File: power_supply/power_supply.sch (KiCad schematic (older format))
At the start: 16 parts, among them J1 Conn_01x02_Female, J6 Conn_01x02_Male, J7 Conn_01x02_Male, T1 Transformer_1P_2S

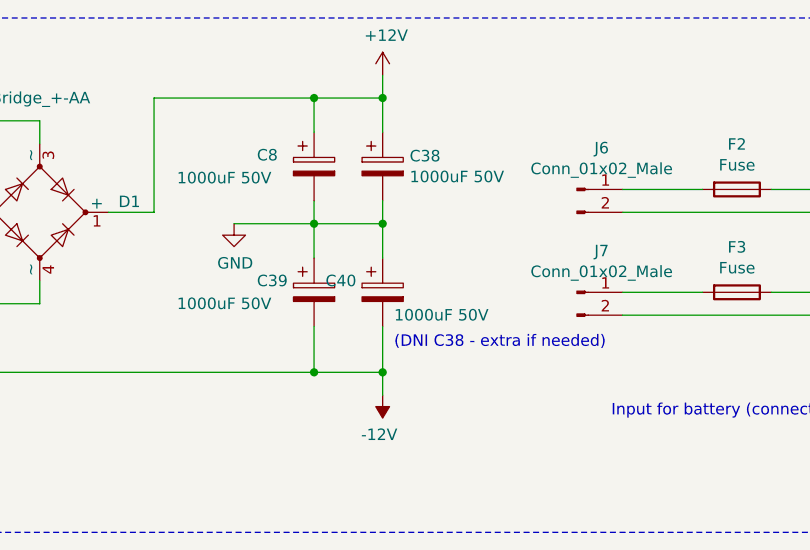
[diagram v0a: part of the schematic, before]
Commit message: Moved power supply off preamp
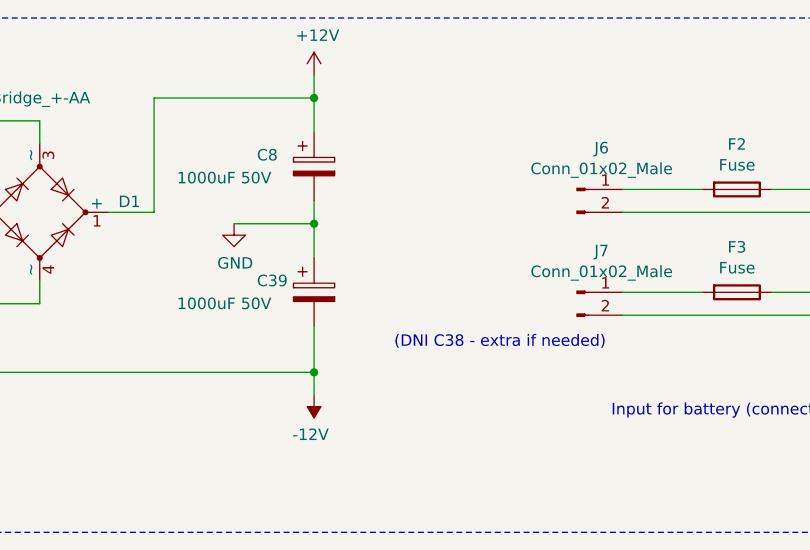
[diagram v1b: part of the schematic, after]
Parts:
- removed C38, C40: 1000uF 50V, Capacitor_THT:CP_Radial_D17.0mm_P7.50mm, symbol Device:CP
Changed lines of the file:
@@
 Wire Wire Line
 	5600 2000 5600 2200
-Wire Wire Line
-	5600 2200 5900 2200
 $Comp
 L Device:Transformer_1P_2S T1
@@
 L power:+12V #PWR0102
 U 1 1 5D654E8A
-P 5900 900
-F 0 "#PWR0102" H 5900 750 50  0001 C CNN
-F 1 "+12V" H 5915 1073 50  0000 C CNN
-F 2 "" H 5900 900 50  0001 C CNN
-F 3 "" H 5900 900 50  0001 C CNN
-	1    5900 900
+P 5600 900
+F 0 "#PWR0102" H 5600 750 50  0001 C CNN
+F 1 "+12V" H 5615 1073 50  0000 C CNN
+F 2 "" H 5600 900 50  0001 C CNN
+F 3 "" H 5600 900 50  0001 C CNN
+	1    5600 900
 	1    0    0    -1
 $EndComp
@@
 L power:-12V #PWR0103
 U 1 1 5D6561DF
-P 5900 2300
-F 0 "#PWR0103" H 5900 2400 50  0001 C CNN
-F 1 "-12V" H 5915 2473 50  0000 C CNN
-F 2 "" H 5900 2300 50  0001 C CNN
-F 3 "" H 5900 2300 50  0001 C CNN
-	1    5900 2300
+P 5600 2300
+F 0 "#PWR0103" H 5600 2400 50  0001 C CNN
+F 1 "-12V" H 5615 2473 50  0000 C CNN
+F 2 "" H 5600 2300 50  0001 C CNN
+F 3 "" H 5600 2300 50  0001 C CNN
+	1    5600 2300
 	-1   0    0    1
 $EndComp
@@
 	0    1    1    0
 $EndComp
-Connection ~ 5600 2200
 Wire Wire Line
 	6950 1400 7300 1400
@@
 Wire Wire Line
 	6950 1950 7850 1950
-$Comp
-L Device:CP C38
-U 1 1 5E1D3B0E
-P 5900 1300
-F 0 "C38" H 6018 1346 50  0000 L CNN
-F 1 "1000uF 50V" H 6018 1255 50  0000 L CNN
-F 2 "Capacitor_THT:CP_Radial_D17.0mm_P7.50mm" H 5938 1150 50  0001 C CNN
-F 3 "~" H 5900 1300 50  0001 C CNN
-	1    5900 1300
-	1    0    0    -1
-$EndComp
 Text Notes 5950 2100 0    50   ~ 0
 (DNI C38 - extra if needed)
-Wire Wire Line
-	5900 2000 5900 2200
-Connection ~ 5900 2200
-Wire Wire Line
-	5900 2300 5900 2200
 Wire Wire Line
 	4700 1500 4900 1500
@@
 	1    0    0    -1
 $EndComp
-$Comp
-L Device:CP C40
-U 1 1 5E00BF29
-P 5900 1850
-F 0 "C40" H 5650 1900 50  0000 L CNN
-F 1 "1000uF 50V" H 5950 1750 50  0000 L CNN
-F 2 "Capacitor_THT:CP_Radial_D17.0mm_P7.50mm" H 5938 1700 50  0001 C CNN
-F 3 "~" H 5900 1850 50  0001 C CNN
-	1    5900 1850
-	1    0    0    -1
-$EndComp
-Wire Wire Line
-	5900 1450 5900 1550
 Wire Wire Line
 	5600 1700 5600 1550
 Wire Wire Line
-	5900 1000 5900 1150
-Wire Wire Line
 	5600 1150 5600 1000
-Connection ~ 5600 1000
-Wire Wire Line
-	5600 1000 5900 1000
 $Comp
 L power:GND #PWR0215
@@
 Wire Wire Line
 	5600 1550 5600 1450
-Wire Wire Line
-	5600 1550 5900 1550
-Connection ~ 5900 1550
-Wire Wire Line
-	5900 1550 5900 1700
-Wire Wire Line
-	5900 900  5900 1000
-Connection ~ 5900 1000
 Wire Wire Line
 	4900 1000 5600 1000
@@
 Wire Notes Line
 	750  650  750  2900
+Connection ~ 5600 2200
+Wire Wire Line
+	5600 2300 5600 2200
+Wire Wire Line
+	5600 1000 5600 900
+Connection ~ 5600 1000
 $EndSCHEMATC

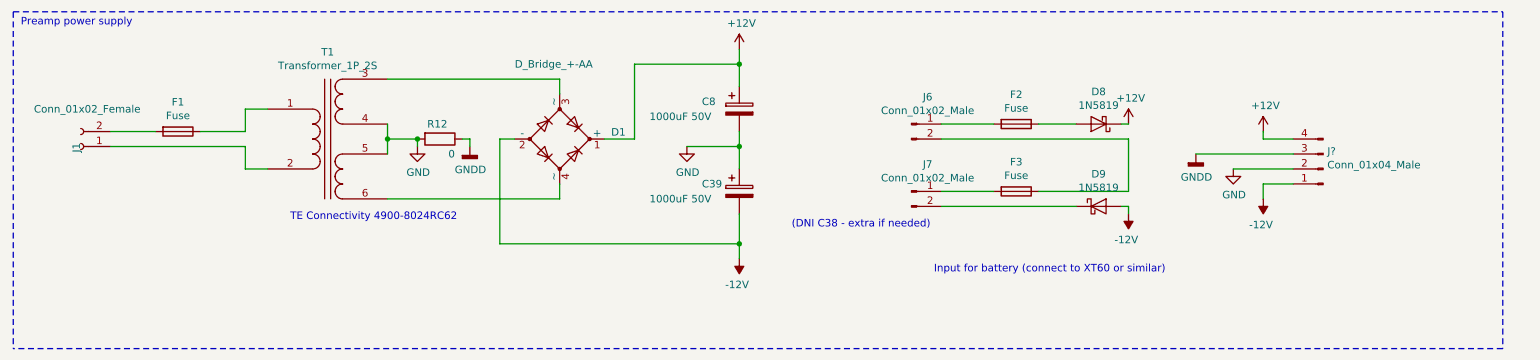
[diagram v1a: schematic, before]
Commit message: Added top-side ground plane, started power supply work
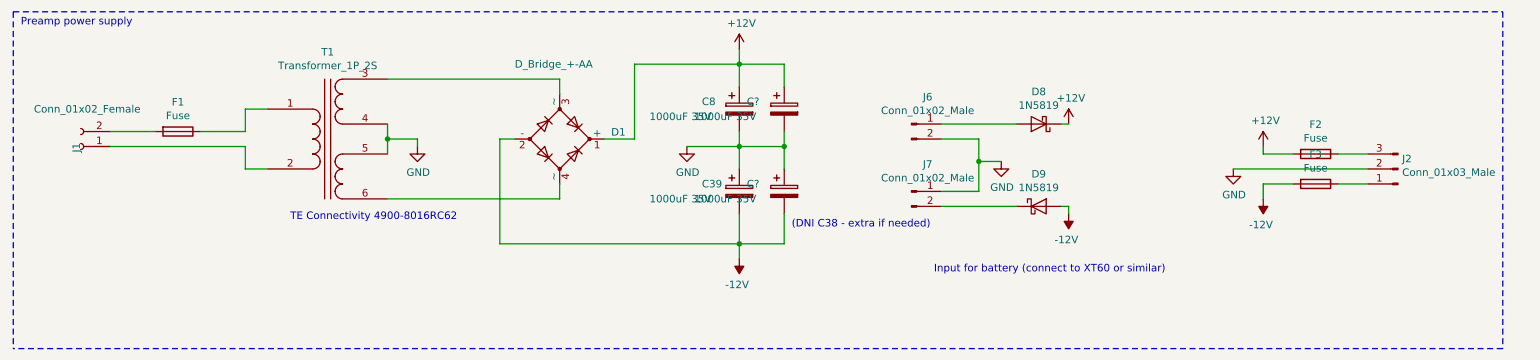
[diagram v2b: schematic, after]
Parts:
- removed J?: Conn_01x04_Male, symbol Connector:Conn_01x04_Male
- removed R12: 0, Resistor_THT:R_Axial_DIN0207_L6.3mm_D2.5mm_P10.16mm_Horizontal, symbol Device:R
- added C? (x2): 1000uF 35V, Capacitor_THT:CP_Radial_D10.0mm_P5.00mm, symbol Device:CP
- added J2: Conn_01x03_Male, Connector_PinHeader_2.54mm:PinHeader_1x03_P2.54mm_Vertical, symbol Connector:Conn_01x03_Male
- C39, C8: value 1000uF 50V -> 1000uF 35V; footprint Capacitor_THT:CP_Radial_D17.0mm_P7.50mm -> Capacitor_THT:CP_Radial_D10.0mm_P5.00mm
- D1: footprint (none) -> Project-152-Bass-Guitar-Amp.pretty:DiodesIncDF-M
- F2, F3: footprint (none) -> Fuse:Fuseholder_Blade_Mini_Keystone_3568
- T1: footprint Project-152-Bass-Guitar-Amp:TE 49008024RC62 -> Project-152-Bass-Guitar-Amp.pretty:TE490080XXRC62
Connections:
- net +12V: now also F2.2, C?.1
- net -12V: now also F3.2, C?.2
- net GND: now also J6.2 (Pin_2), J7.1 (Pin_1), C?.1, C?.2, J2.2 (Pin_2)
- net at J6.1 (Pin_1): now also D8.2 (A); no longer F2.2
- net at F3.1: now also J2.1 (Pin_1); no longer J6.2 (Pin_2)
- net at F2.1: now also J2.3 (Pin_3); no longer D8.2 (A)
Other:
- note added: "TE Connectivity 4900-8016RC62"
- note removed: "TE Connectivity 4900-8024RC62"
- moved on the sheet: D8, D9, F2, F3
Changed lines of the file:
@@
 F 0 "D1" H 4744 1546 50  0000 L CNN
 F 1 "D_Bridge_+-AA" H 4100 2000 50  0000 L CNN
-F 2 "" H 4400 1500 50  0001 C CNN
+F 2 "Project-152-Bass-Guitar-Amp.pretty:DiodesIncDF-M" H 4400 1500 50  0001 C CNN
 F 3 "~" H 4400 1500 50  0001 C CNN
 	1    4400 1500
@@
 	4000 1500 4000 2200
 Text Notes 2600 2050 0    50   ~ 0
-TE Connectivity 4900-8024RC62
+TE Connectivity 4900-8016RC62
 $Comp
 L Connector:Conn_01x02_Female J1
@@
 P 5600 1300
 F 0 "C8" H 5350 1350 50  0000 L CNN
-F 1 "1000uF 50V" H 5000 1250 50  0000 L CNN
-F 2 "Capacitor_THT:CP_Radial_D17.0mm_P7.50mm" H 5638 1150 50  0001 C CNN
+F 1 "1000uF 35V" H 5000 1250 50  0000 L CNN
+F 2 "Capacitor_THT:CP_Radial_D10.0mm_P5.00mm" H 5638 1150 50  0001 C CNN
 F 3 "~" H 5600 1300 50  0001 C CNN
 	1    5600 1300
@@
 F 0 "T1" H 2850 2081 50  0000 C CNN
 F 1 "Transformer_1P_2S" H 2850 1990 50  0000 C CNN
-F 2 "Project-152-Bass-Guitar-Amp:TE 49008024RC62" H 2850 1500 50  0001 C CNN
+F 2 "Project-152-Bass-Guitar-Amp.pretty:TE490080XXRC62" H 2850 1500 50  0001 C CNN
 F 3 "~" H 2850 1500 50  0001 C CNN
 	1    2850 1500
@@
 	1    0    0    -1
 $EndComp
-Wire Wire Line
-	8200 1500 8200 1850
 $Comp
 L power:+12V #PWR0118
 U 1 1 5D6AE19B
-P 8200 1400
-F 0 "#PWR0118" H 8200 1250 50  0001 C CNN
-F 1 "+12V" H 8215 1573 50  0000 C CNN
-F 2 "" H 8200 1400 50  0001 C CNN
-F 3 "" H 8200 1400 50  0001 C CNN
-	1    8200 1400
+P 7800 1400
+F 0 "#PWR0118" H 7800 1250 50  0001 C CNN
+F 1 "+12V" H 7815 1573 50  0000 C CNN
+F 2 "" H 7800 1400 50  0001 C CNN
+F 3 "" H 7800 1400 50  0001 C CNN
+	1    7800 1400
 	1    0    0    -1
 $EndComp
@@
 L power:-12V #PWR0119
 U 1 1 5D6AED97
-P 8200 2000
-F 0 "#PWR0119" H 8200 2100 50  0001 C CNN
-F 1 "-12V" H 8215 2173 50  0000 C CNN
-F 2 "" H 8200 2000 50  0001 C CNN
-F 3 "" H 8200 2000 50  0001 C CNN
-	1    8200 2000
-	-1   0    0    1
-$EndComp
-Wire Wire Line
-	8200 1950 8200 2000
-Wire Wire Line
-	7600 1850 8200 1850
-Wire Wire Line
-	7600 1400 7850 1400
+P 7800 2000
+F 0 "#PWR0119" H 7800 2100 50  0001 C CNN
+F 1 "-12V" H 7815 2173 50  0000 C CNN
+F 2 "" H 7800 2000 50  0001 C CNN
+F 3 "" H 7800 2000 50  0001 C CNN
+	1    7800 2000
+	-1   0    0    1
+$EndComp
+Wire Wire Line
+	7800 1950 7800 2000
 Text Notes 6900 2400 0    50   ~ 0
 Input for battery (connect to XT60 or similar)
 Wire Wire Line
-	8150 1950 8200 1950
+	7750 1950 7800 1950
 $Comp
 L Diode:1N5819 D8
 U 1 1 5D6CDB80
-P 8000 1400
-F 0 "D8" H 8000 1184 50  0000 C CNN
-F 1 "1N5819" H 8000 1275 50  0000 C CNN
-F 2 "Diode_THT:D_DO-41_SOD81_P10.16mm_Horizontal" H 8000 1225 50  0001 C CNN
-F 3 "http://www.vishay.com/docs/88525/1n5817.pdf" H 8000 1400 50  0001 C CNN
-	1    8000 1400
+P 7600 1400
+F 0 "D8" H 7600 1184 50  0000 C CNN
+F 1 "1N5819" H 7600 1275 50  0000 C CNN
+F 2 "Diode_THT:D_DO-41_SOD81_P10.16mm_Horizontal" H 7600 1225 50  0001 C CNN
+F 3 "http://www.vishay.com/docs/88525/1n5817.pdf" H 7600 1400 50  0001 C CNN
+	1    7600 1400
 	-1   0    0    1
 $EndComp
@@
 L Diode:1N5819 D9
 U 1 1 5D6CF15E
-P 8000 1950
-F 0 "D9" H 8000 2166 50  0000 C CNN
-F 1 "1N5819" H 8000 2075 50  0000 C CNN
-F 2 "Diode_THT:D_DO-41_SOD81_P10.16mm_Horizontal" H 8000 1775 50  0001 C CNN
-F 3 "http://www.vishay.com/docs/88525/1n5817.pdf" H 8000 1950 50  0001 C CNN
-	1    8000 1950
-	1    0    0    -1
-$EndComp
-Wire Wire Line
-	8200 1400 8150 1400
+P 7600 1950
+F 0 "D9" H 7600 2166 50  0000 C CNN
+F 1 "1N5819" H 7600 2075 50  0000 C CNN
+F 2 "Diode_THT:D_DO-41_SOD81_P10.16mm_Horizontal" H 7600 1775 50  0001 C CNN
+F 3 "http://www.vishay.com/docs/88525/1n5817.pdf" H 7600 1950 50  0001 C CNN
+	1    7600 1950
+	1    0    0    -1
+$EndComp
+Wire Wire Line
+	7800 1400 7750 1400
 Text Notes 800  750  0    50   ~ 0
 Preamp power supply
@@
 	1400 1550 2300 1550
 $Comp
-L power:GNDD #PWR0145
-U 1 1 5D854759
-P 3800 1550
-F 0 "#PWR0145" H 3800 1300 50  0001 C CNN
-F 1 "GNDD" H 3804 1395 50  0000 C CNN
-F 2 "" H 3800 1550 50  0001 C CNN
-F 3 "" H 3800 1550 50  0001 C CNN
-	1    3800 1550
-	1    0    0    -1
-$EndComp
-Wire Wire Line
-	3800 1500 3800 1550
-$Comp
-L Device:R R12
-U 1 1 5D8EA5F3
-P 3600 1500
-F 0 "R12" V 3500 1550 50  0000 R CNN
-F 1 "0" V 3700 1600 50  0000 R CNN
-F 2 "Resistor_THT:R_Axial_DIN0207_L6.3mm_D2.5mm_P10.16mm_Horizontal" V 3530 1500 50  0001 C CNN
-F 3 "~" H 3600 1500 50  0001 C CNN
-	1    3600 1500
-	0    1    1    0
-$EndComp
-Connection ~ 3450 1500
-Wire Wire Line
-	3750 1500 3800 1500
-$Comp
 L Device:Fuse F2
 U 1 1 5E48268A
-P 7450 1400
-F 0 "F2" V 7253 1400 50  0000 C CNN
-F 1 "Fuse" V 7344 1400 50  0000 C CNN
-F 2 "" V 7380 1400 50  0001 C CNN
-F 3 "~" H 7450 1400 50  0001 C CNN
-	1    7450 1400
+P 9450 1600
+F 0 "F2" V 9253 1600 50  0000 C CNN
+F 1 "Fuse" V 9344 1600 50  0000 C CNN
+F 2 "Fuse:Fuseholder_Blade_Mini_Keystone_3568" V 9380 1600 50  0001 C CNN
+F 3 "~" H 9450 1600 50  0001 C CNN
+	1    9450 1600
 	0    1    1    0
 $EndComp
@@
 L Device:Fuse F3
 U 1 1 5E4FFBD7
-P 7450 1850
-F 0 "F3" V 7253 1850 50  0000 C CNN
-F 1 "Fuse" V 7344 1850 50  0000 C CNN
-F 2 "" V 7380 1850 50  0001 C CNN
-F 3 "~" H 7450 1850 50  0001 C CNN
-	1    7450 1850
+P 9450 1800
+F 0 "F3" V 9253 1800 50  0000 C CNN
+F 1 "Fuse" V 9344 1800 50  0000 C CNN
+F 2 "Fuse:Fuseholder_Blade_Mini_Keystone_3568" V 9380 1800 50  0001 C CNN
+F 3 "~" H 9450 1800 50  0001 C CNN
+	1    9450 1800
 	0    1    1    0
 $EndComp
-Wire Wire Line
-	6950 1400 7300 1400
-Wire Wire Line
-	6950 1500 8200 1500
-Wire Wire Line
-	6950 1850 7300 1850
-Wire Wire Line
-	6950 1950 7850 1950
 Text Notes 5950 2100 0    50   ~ 0
 (DNI C38 - extra if needed)
@@
 P 5600 1850
 F 0 "C39" H 5350 1900 50  0000 L CNN
-F 1 "1000uF 50V" H 5000 1800 50  0000 L CNN
-F 2 "Capacitor_THT:CP_Radial_D17.0mm_P7.50mm" H 5638 1700 50  0001 C CNN
+F 1 "1000uF 35V" H 5000 1800 50  0000 L CNN
+F 2 "Capacitor_THT:CP_Radial_D10.0mm_P5.00mm" H 5638 1700 50  0001 C CNN
 F 3 "~" H 5600 1850 50  0001 C CNN
 	1    5600 1850
@@
 	4000 2200 5600 2200
 $Comp
-L Connector:Conn_01x04_Male J?
-U 1 1 5E223555
-P 9500 1700
-F 0 "J?" H 9472 1582 50  0000 R CNN
-F 1 "Conn_01x04_Male" H 9472 1673 50  0000 R CNN
-F 2 "" H 9500 1700 50  0001 C CNN
-F 3 "~" H 9500 1700 50  0001 C CNN
-	1    9500 1700
-	-1   0    0    1
-$EndComp
-$Comp
-L power:+12V #PWR?
+L power:+12V #PWR0104
 U 1 1 5E225013
-P 9100 1450
-F 0 "#PWR?" H 9100 1300 50  0001 C CNN
-F 1 "+12V" H 9115 1623 50  0000 C CNN
-F 2 "" H 9100 1450 50  0001 C CNN
-F 3 "" H 9100 1450 50  0001 C CNN
-	1    9100 1450
-	1    0    0    -1
-$EndComp
-$Comp
-L power:-12V #PWR?
+P 9100 1550
+F 0 "#PWR0104" H 9100 1400 50  0001 C CNN
+F 1 "+12V" H 9115 1723 50  0000 C CNN
+F 2 "" H 9100 1550 50  0001 C CNN
+F 3 "" H 9100 1550 50  0001 C CNN
+	1    9100 1550
+	1    0    0    -1
+$EndComp
+$Comp
+L power:-12V #PWR0105
 U 1 1 5E2257B1
 P 9100 1900
-F 0 "#PWR?" H 9100 2000 50  0001 C CNN
+F 0 "#PWR0105" H 9100 2000 50  0001 C CNN
 F 1 "-12V" H 9115 2073 50  0000 C CNN
 F 2 "" H 9100 1900 50  0001 C CNN
@@
 	9100 1800 9100 1900
 Wire Wire Line
-	9300 1500 9100 1500
-Wire Wire Line
-	9100 1500 9100 1450
-$Comp
-L power:GND #PWR?
+	9300 1600 9100 1600
+Wire Wire Line
+	9100 1600 9100 1550
+$Comp
+L power:GND #PWR0106
 U 1 1 5E22769F
 P 8900 1700
-F 0 "#PWR?" H 8900 1450 50  0001 C CNN
+F 0 "#PWR0106" H 8900 1450 50  0001 C CNN
 F 1 "GND" H 8905 1527 50  0000 C CNN
 F 2 "" H 8900 1700 50  0001 C CNN
@@
 	1    0    0    -1
 $EndComp
-$Comp
-L power:GNDD #PWR?
-U 1 1 5E227A52
-P 8650 1600
-F 0 "#PWR?" H 8650 1350 50  0001 C CNN
-F 1 "GNDD" H 8654 1445 50  0000 C CNN
-F 2 "" H 8650 1600 50  0001 C CNN
-F 3 "" H 8650 1600 50  0001 C CNN
-	1    8650 1600
-	1    0    0    -1
-$EndComp
-Wire Wire Line
-	9300 1600 8650 1600
-Wire Wire Line
-	8900 1700 9300 1700
 Wire Notes Line
 	750  650  10700 650
@@
 	5600 1000 5600 900
 Connection ~ 5600 1000
+$Comp
+L Connector:Conn_01x03_Male J2
+U 1 1 5E52B3B7
+P 10000 1700
+F 0 "J2" H 9972 1632 50  0000 R CNN
+F 1 "Conn_01x03_Male" H 9972 1723 50  0000 R CNN
+F 2 "Connector_PinHeader_2.54mm:PinHeader_1x03_P2.54mm_Vertical" H 10000 1700 50  0001 C CNN
+F 3 "~" H 10000 1700 50  0001 C CNN
+	1    10000 1700
+	-1   0    0    1
+$EndComp
+Wire Wire Line
+	8900 1700 9800 1700
+Wire Wire Line
+	9600 1600 9800 1600
+Wire Wire Line
+	9800 1800 9600 1800
+$Comp
+L power:GND #PWR0107
+U 1 1 5E53085C
+P 7350 1650
+F 0 "#PWR0107" H 7350 1400 50  0001 C CNN
+F 1 "GND" H 7355 1477 50  0000 C CNN
+F 2 "" H 7350 1650 50  0001 C CNN
+F 3 "" H 7350 1650 50  0001 C CNN
+	1    7350 1650
+	1    0    0    -1
+$EndComp
+Wire Wire Line
+	7350 1650 7200 1650
+Wire Wire Line
+	6950 1500 7200 1500
+Wire Wire Line
+	7200 1500 7200 1650
+Wire Wire Line
+	7200 1850 6950 1850
+Connection ~ 7200 1650
+Wire Wire Line
+	7200 1650 7200 1850
+Wire Wire Line
+	6950 1400 7450 1400
+Wire Wire Line
+	6950 1950 7450 1950
+$Comp
+L Device:CP C?
+U 1 1 5E53BAB1
+P 5900 1300
+F 0 "C?" H 5650 1350 50  0000 L CNN
+F 1 "1000uF 35V" H 5300 1250 50  0000 L CNN
+F 2 "Capacitor_THT:CP_Radial_D10.0mm_P5.00mm" H 5938 1150 50  0001 C CNN
+F 3 "~" H 5900 1300 50  0001 C CNN
+	1    5900 1300
+	1    0    0    -1
+$EndComp
+$Comp
+L Device:CP C?
+U 1 1 5E53BD92
+P 5900 1850
+F 0 "C?" H 5650 1900 50  0000 L CNN
+F 1 "1000uF 35V" H 5300 1800 50  0000 L CNN
+F 2 "Capacitor_THT:CP_Radial_D10.0mm_P5.00mm" H 5938 1700 50  0001 C CNN
+F 3 "~" H 5900 1850 50  0001 C CNN
+	1    5900 1850
+	1    0    0    -1
+$EndComp
+Wire Wire Line
+	5900 1700 5900 1550
+Wire Wire Line
+	5900 1550 5600 1550
+Wire Wire Line
+	5900 1450 5900 1550
+Connection ~ 5900 1550
+Wire Wire Line
+	5600 1000 5900 1000
+Wire Wire Line
+	5900 1000 5900 1150
+Wire Wire Line
+	5600 2200 5900 2200
+Wire Wire Line
+	5900 2200 5900 2000
 $EndSCHEMATC

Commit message: More layout
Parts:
- added H1, H2, H3, H4: MountingHole, MountingHole:MountingHole_3.2mm_M3_DIN965, symbol Mechanical:MountingHole
- F1: footprint Fuse:Fuseholder_Cylinder-5x20mm_Schurter_0031-8002_Horizontal_Open -> Project-152-Bass-Guitar-Amp.pretty:Keystone-3527-Fuseholder
- gave numbers to parts that had none: 2
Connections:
- net at T1.3 (SA): now also D1.4 (~~); no longer D1.3 (~~)
- net at T1.6 (SD): now also D1.3 (~~); no longer D1.4 (~~)
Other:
- moved on the sheet: C1, C2, C39, C8, D1, F1, J1, T1

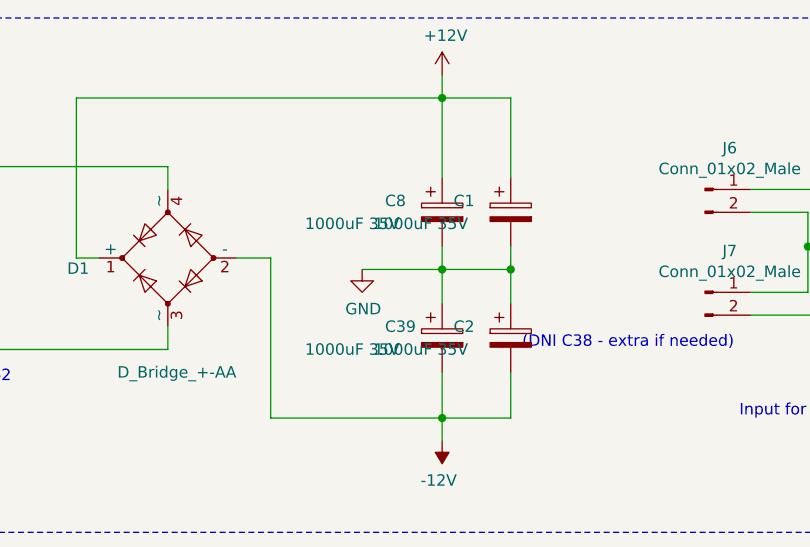
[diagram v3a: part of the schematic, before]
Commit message: Finished power supply layout, sent out for first rev of boards
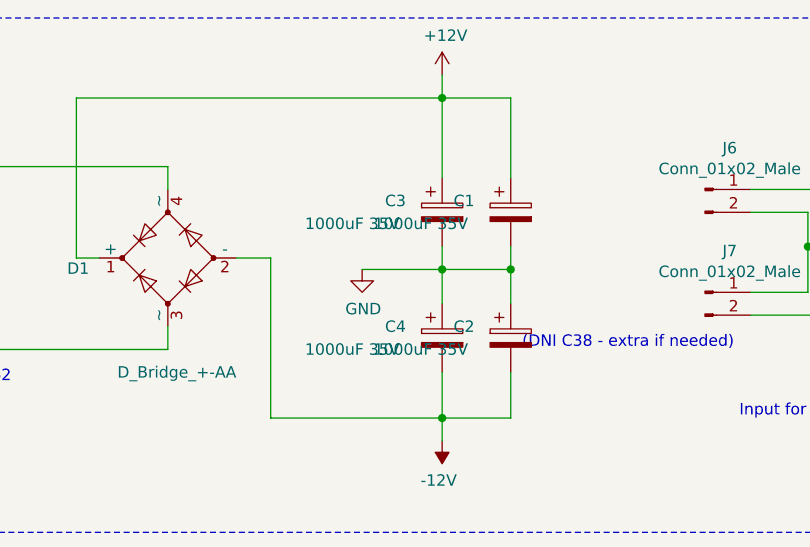
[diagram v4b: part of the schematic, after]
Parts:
- renumbered C8 to C3, C39 to C4
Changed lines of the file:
@@
 	2300 1900 2450 1900
 $Comp
-L Device:CP C8
+L Device:CP C3
 U 1 1 5D649C46
 P 5600 1500
-F 0 "C8" H 5350 1550 50  0000 L CNN
+F 0 "C3" H 5350 1550 50  0000 L CNN
 F 1 "1000uF 35V" H 5000 1450 50  0000 L CNN
 F 2 "Capacitor_THT:CP_Radial_D10.0mm_P5.00mm" H 5638 1350 50  0001 C CNN
@@
 (DNI C38 - extra if needed)
 $Comp
-L Device:CP C39
+L Device:CP C4
 U 1 1 5E00BA06
 P 5600 2050
-F 0 "C39" H 5350 2100 50  0000 L CNN
+F 0 "C4" H 5350 2100 50  0000 L CNN
 F 1 "1000uF 35V" H 5000 2000 50  0000 L CNN
 F 2 "Capacitor_THT:CP_Radial_D10.0mm_P5.00mm" H 5638 1900 50  0001 C CNN
